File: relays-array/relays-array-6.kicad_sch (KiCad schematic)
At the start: 50 parts, among them J1 NMJ6HCD2, J10 Screw_Terminal_01x02, J14 NMJ6HCD2, J15 Screw_Terminal_01x02, J2 NMJ6HCD2, J3 Screw_Terminal_01x02, J4 NMJ6HCD2, J5 NMJ6HCD2, J6 Screw_Terminal_01x02, J7 NMJ6HCD2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

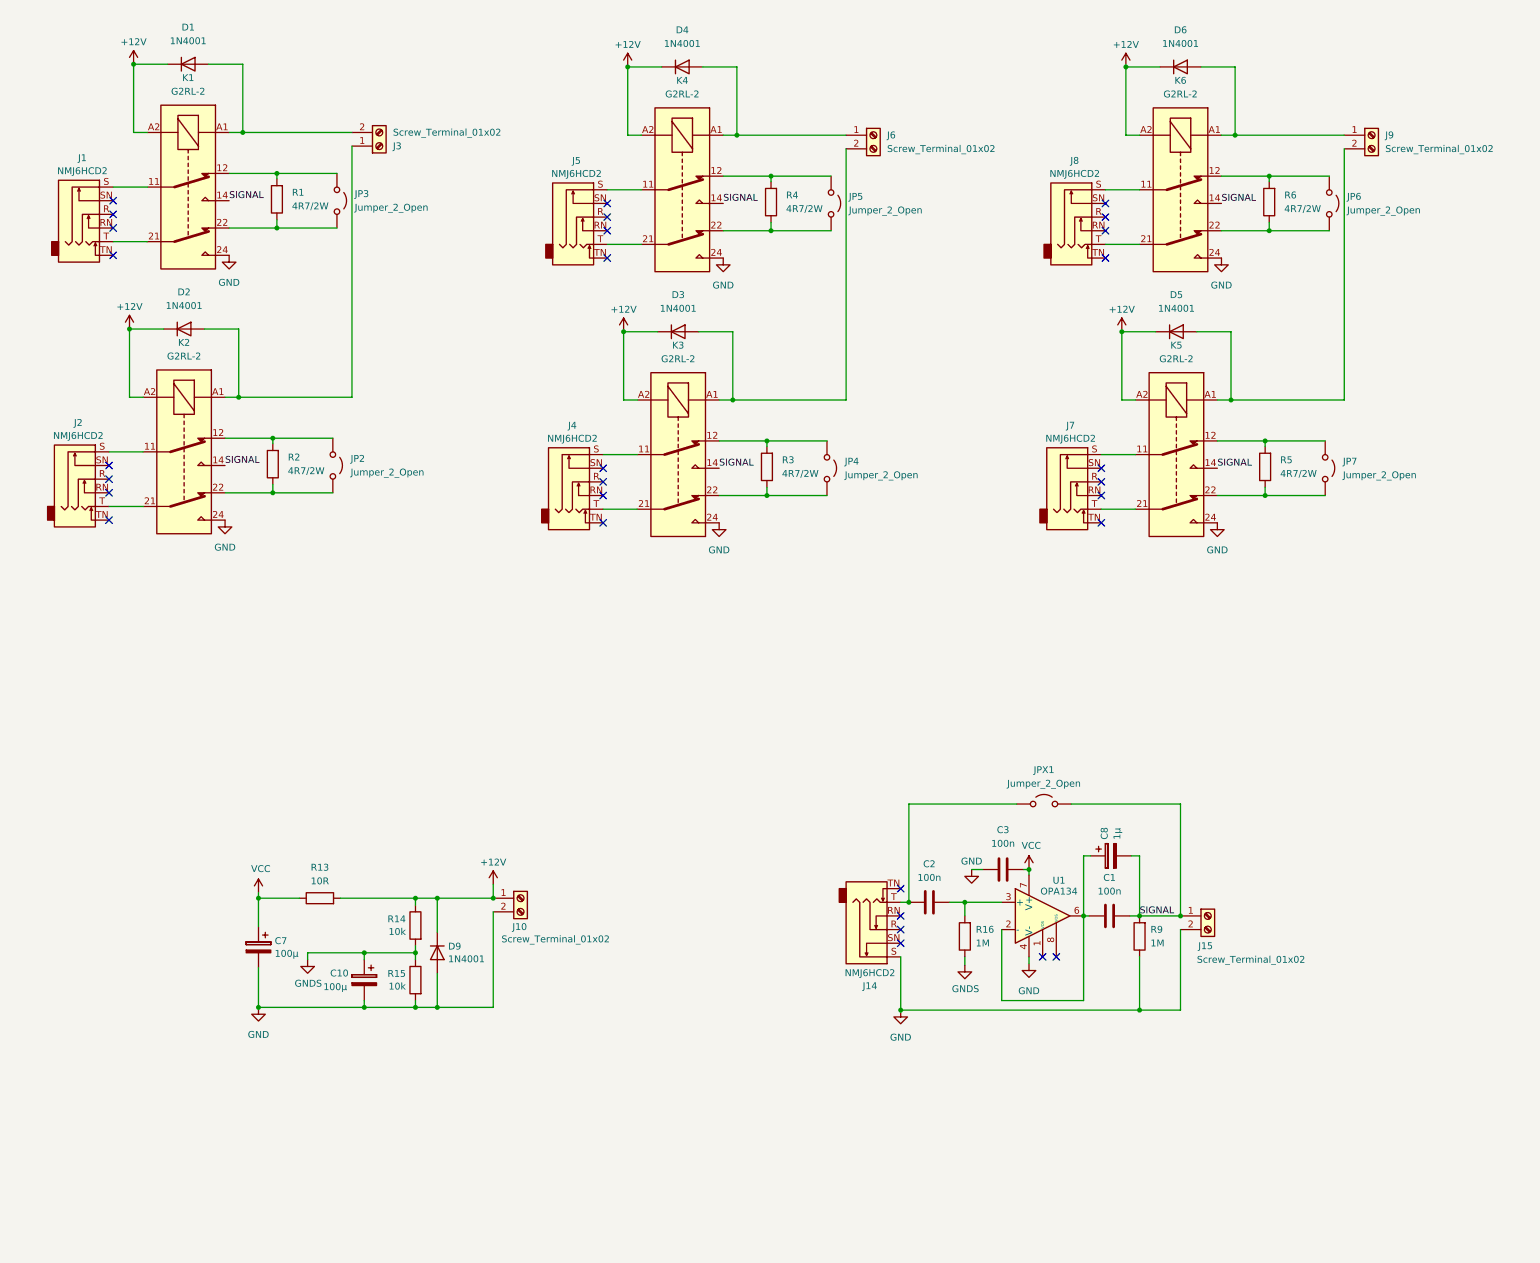
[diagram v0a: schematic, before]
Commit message: relays-array: add terminal block for buffer use w/ external connector
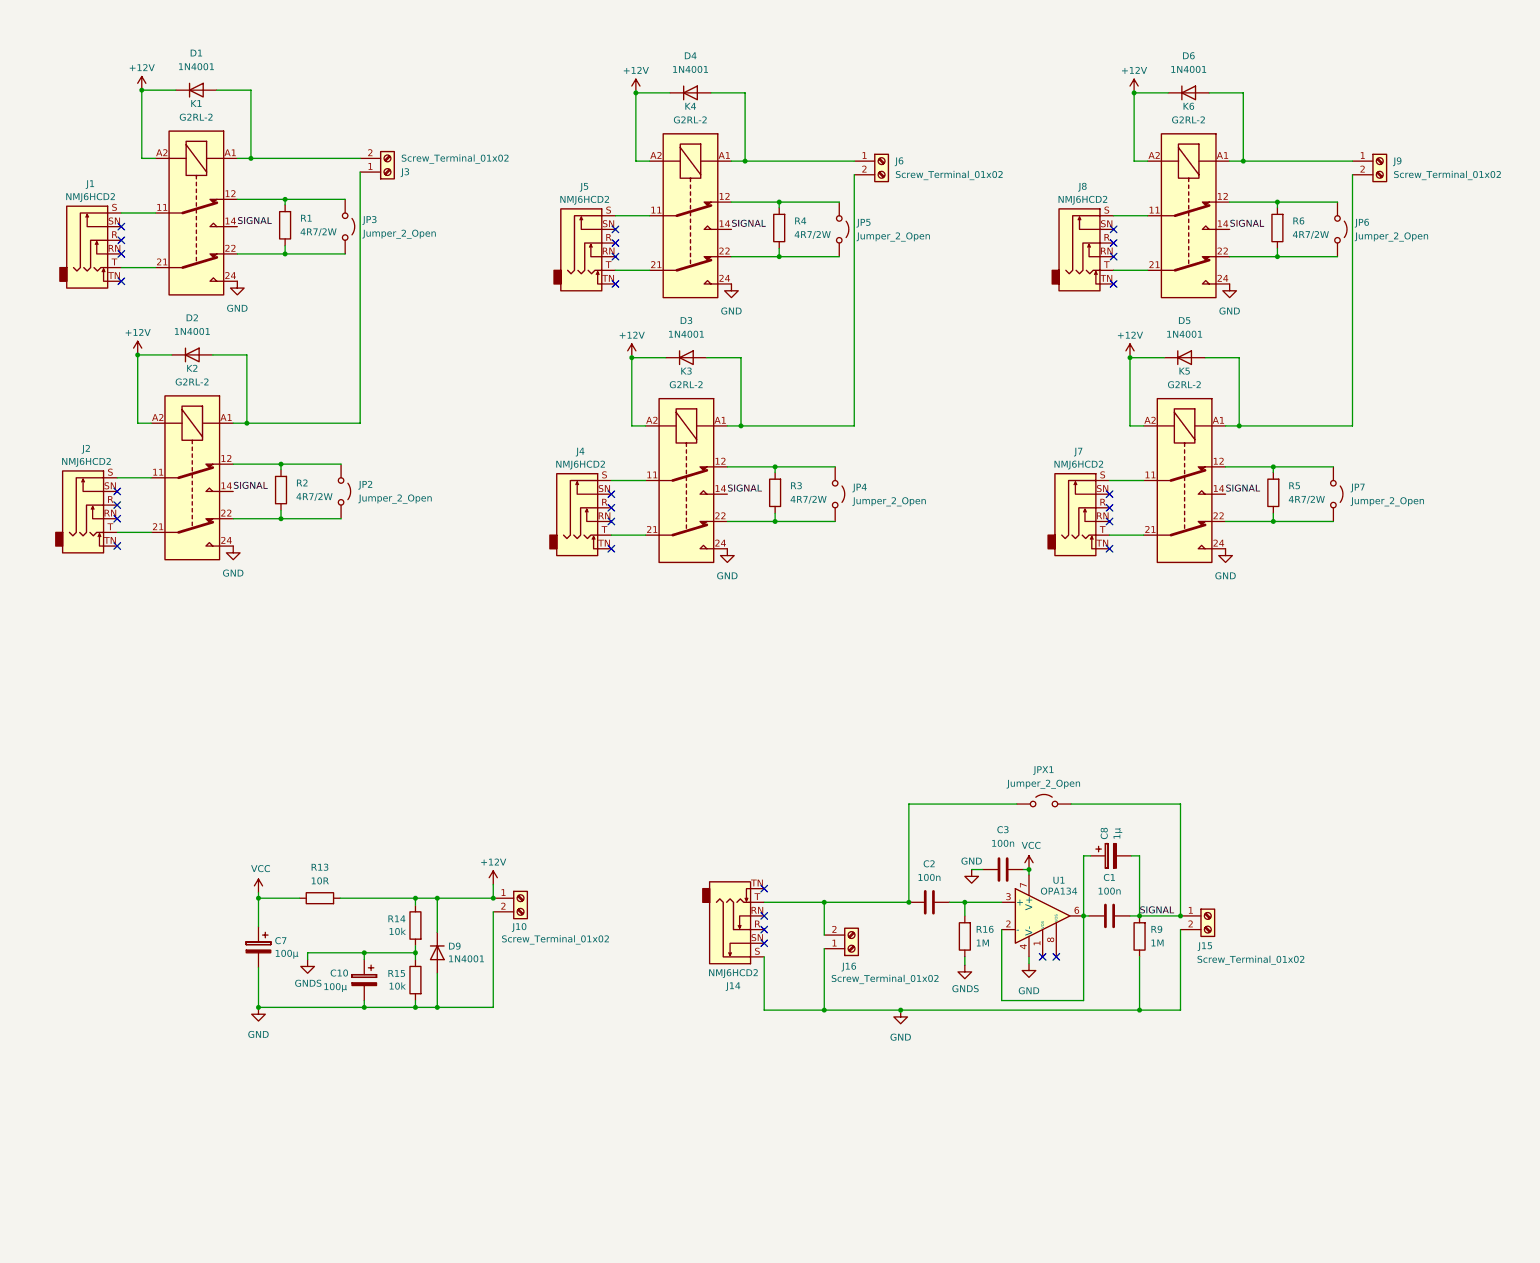
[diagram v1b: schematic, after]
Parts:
- added J16: Screw_Terminal_01x02, TerminalBlock:TerminalBlock_bornier-2_P5.08mm, symbol Connector:Screw_Terminal_01x02
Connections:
- net GND: now also J16.1 (Pin_1)
- net at C2.2, J14.T, JPX1.2 (B): now also J16.2 (Pin_2)
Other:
- moved on the sheet: D1, D2, D3, D4, D5, D6, J1, J14, J2, J3, J4, J5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

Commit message: relays-array: fix schematics error and add ground plane
The jack connectors are all (except for the buffer input) wired
backwards, with the tip going to `GND` and the sleeve on `SIGNAL`, while
it should be the other way around.

While at it, improve a bit the PCB tracks and add a ground plane. The
latter is only connected to `GND` in a single point in order to avoid
ground loops and other unpleasant issues.
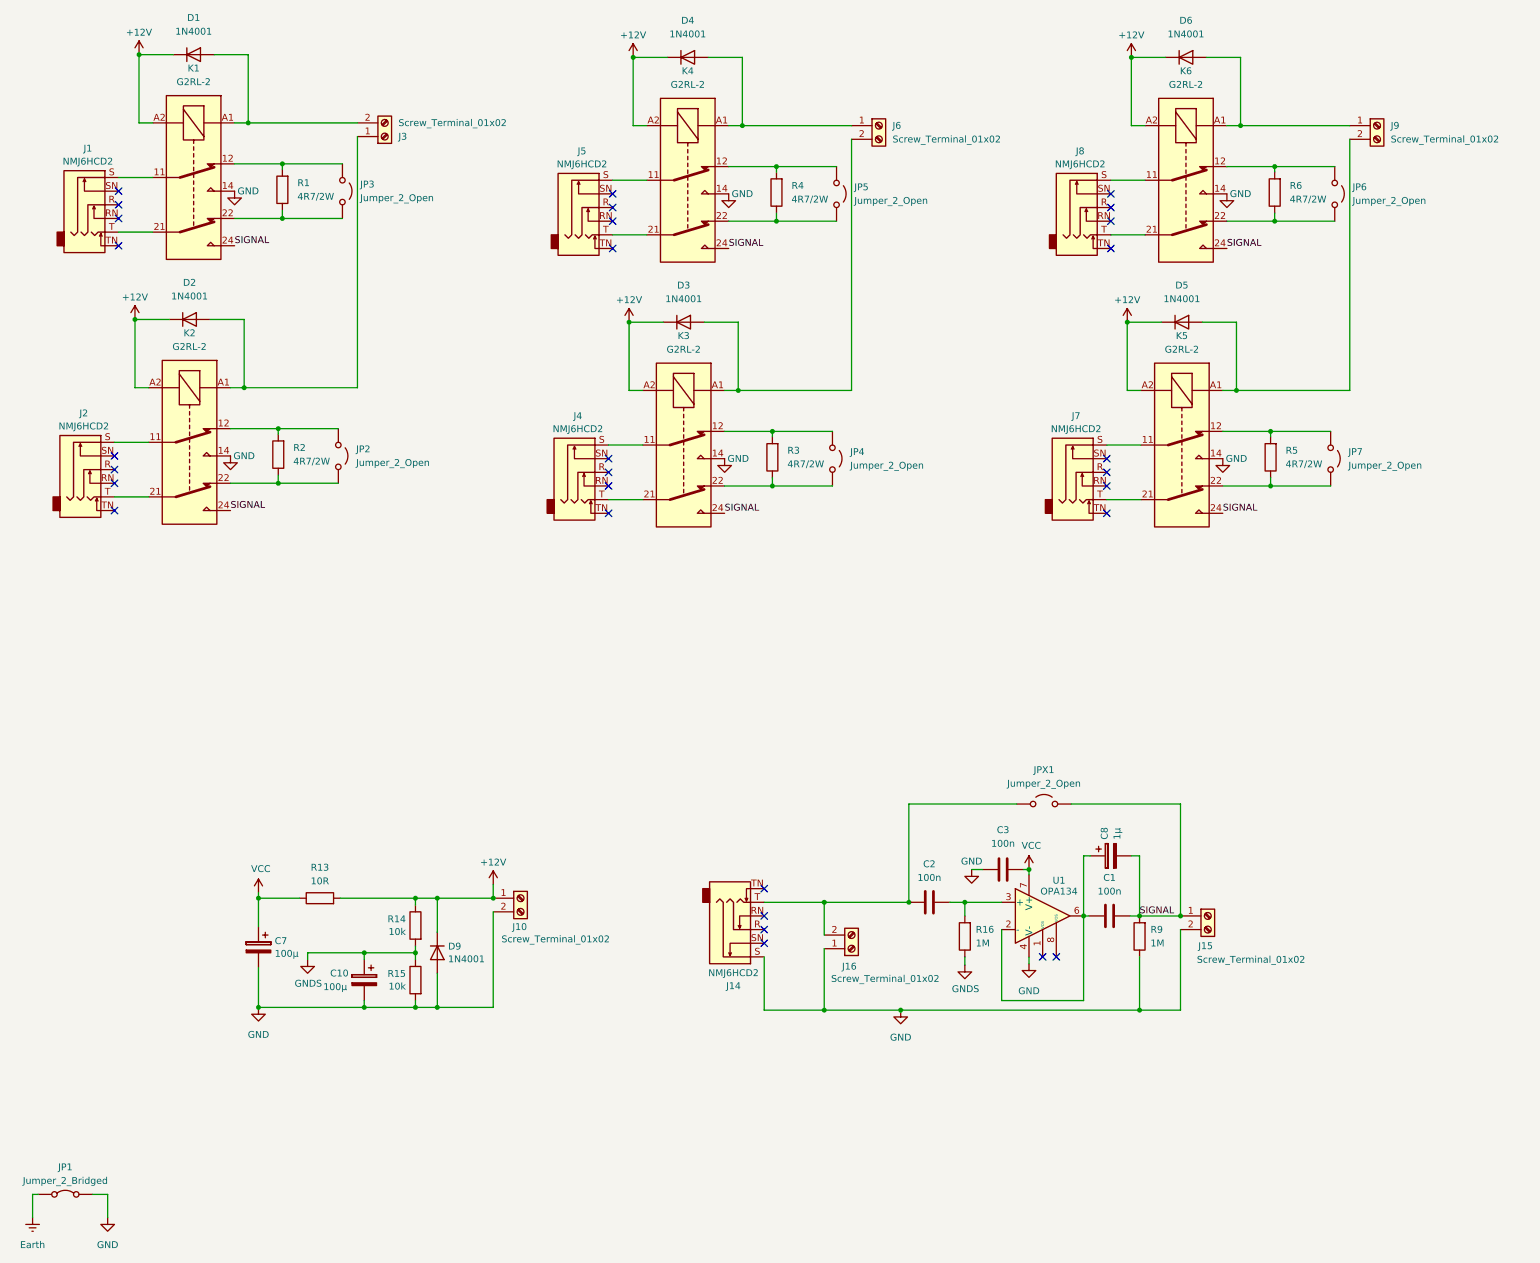
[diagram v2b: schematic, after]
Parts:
- added JP1: Jumper_2_Bridged, Jumper:SolderJumper-2_P1.3mm_Bridged_RoundedPad1.0x1.5mm, symbol Jumper:Jumper_2_Bridged
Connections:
- net GND: now also K1.14, K2.14, K3.14, K4.14, K5.14, K6.14, JP1.2 (B); no longer K1.24, K2.24, K3.24, K4.24, K5.24, K6.24
- net SIGNAL: now also K1.24, K2.24, K3.24, K4.24, K5.24, K6.24; no longer K1.14, K2.14, K3.14, K4.14, K5.14, K6.14
- new net Earth: JP1.1 (A)
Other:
- moved on the sheet: D1, D2, D3, D4, D5, D6, J1, J2, J3, J4, J5, J6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
